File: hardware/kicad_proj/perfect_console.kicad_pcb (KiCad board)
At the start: 2 copper layers, 70 x 95 mm, 71 parts, among them J1 R_Out, J10 PWR_OUT_Pins, J11 GPIO5-7, J12 USB_Out, J13 I2C, J14 ESP_UART, J15 GPIO41, J16 CH_UART, J17 CH_Flash, J18 Micro_SD_Card, J2 Jack_3.5, J3 L_Out, J4 USB, J5 TP4056_WO_Protect, J6 Bat, J7 PWR_Btn, J8 BTN_Pins, J9 PTT_Btn, Q1 NMOS, Q2 NMOS, Q3 NMOS, Q4 NMOS, Q5 NMOS, Q6 NMOS, SW1 Reset, SW2 Boot, U1 ESP32-S3-WROOM1, U2 Display, U3 PCM5102, U4 PAM8403, U5 CH32V006E8R6, U6 LoRa, U7 USBLC6-2SC6, U8 Mic, U9 DC-DC

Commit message: Виправлено імена міток
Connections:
- net DISP_EN renamed DISP_PWR
- net LORA_EN renamed LORA_PWR
- net MIC_EN renamed MIC_PWR
- net POWER_EN renamed BOARD_PWR
- net SPK_EN renamed SPK_PWR
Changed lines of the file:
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@@
 	(net 6 "Net-(Q2-G)")
 	(net 7 "Net-(Q3-G)")
-	(net 8 "DISP_EN")
+	(net 8 "DISP_PWR")
 	(net 9 "VVAL")
 	(net 10 "Net-(J1-Pin_2)")
@@
 	(net 76 "unconnected-(J18-DAT2-Pad1)")
 	(net 77 "unconnected-(J18-DAT1-Pad8)")
-	(net 78 "SPK_EN")
-	(net 79 "LORA_EN")
-	(net 80 "MIC_EN")
-	(net 81 "POWER_EN")
+	(net 78 "SPK_PWR")
+	(net 79 "LORA_PWR")
+	(net 80 "MIC_PWR")
+	(net 81 "BOARD_PWR")
 	(net 82 "Net-(Q1-D)")
 	(net 83 "Net-(Q2-D)")
@@
 			(layers "F.Cu" "F.Paste" "F.Mask")
 			(roundrect_rratio 0.192308)
-			(net 8 "DISP_EN")
+			(net 8 "DISP_PWR")
 			(pintype "passive")
 		)
@@
 			(size 2.3 0.4)
 			(layers "F.Cu" "F.Paste" "F.Mask")
-			(net 80 "MIC_EN")
+			(net 80 "MIC_PWR")
 			(pinfunction "PD7/T2")
 			(pintype "bidirectional")
@@
 			(size 2.3 0.4)
 			(layers "F.Cu" "F.Paste" "F.Mask")
-			(net 8 "DISP_EN")
+			(net 8 "DISP_PWR")
 			(pinfunction "PA4/U2TX")
 			(pintype "bidirectional")
@@
 			(size 2.3 0.4)
 			(layers "F.Cu" "F.Paste" "F.Mask")
-			(net 81 "POWER_EN")
+			(net 81 "BOARD_PWR")
 			(pinfunction "PA5/U2RX_")
 			(pintype "bidirectional")
@@
 			(size 2.3 0.4)
 			(layers "F.Cu" "F.Paste" "F.Mask")
-			(net 79 "LORA_EN")
+			(net 79 "LORA_PWR")
 			(pinfunction "PA0/T1/T2")
 			(pintype "bidirectional")
@@
 			(size 2.3 0.4)
 			(layers "F.Cu" "F.Paste" "F.Mask")
-			(net 78 "SPK_EN")
+			(net 78 "SPK_PWR")
 			(pinfunction "PB3/SWCK")
 			(pintype "bidirectional")
@@
 			(layers "F.Cu" "F.Paste" "F.Mask")
 			(roundrect_rratio 0.05)
-			(net 47 "Net-(J2-L)")
+			(net 46 "Net-(J2-LN)")
 			(pinfunction "LN")
 			(pintype "output")
@@
 			(layers "F.Cu" "F.Paste" "F.Mask")
 			(roundrect_rratio 0.05)
-			(net 46 "Net-(J2-LN)")
+			(net 47 "Net-(J2-L)")
 			(pinfunction "L")
 			(pintype "input")
@@
 			(layers "F.Cu" "F.Paste" "F.Mask")
 			(roundrect_rratio 0.192308)
-			(net 79 "LORA_EN")
+			(net 79 "LORA_PWR")
 			(pintype "passive")
 		)
@@
 			(size 1.6 3)
 			(layers "F.Cu" "F.Paste" "F.Mask")
-			(net 46 "Net-(J2-LN)")
+			(net 47 "Net-(J2-L)")
 			(pinfunction "LEFT")
 			(pintype "output")
@@
 			(layers "F.Cu" "F.Paste" "F.Mask")
 			(roundrect_rratio 0.192308)
-			(net 81 "POWER_EN")
+			(net 81 "BOARD_PWR")
 			(pintype "passive")
 		)
@@
 			(layers "B.Cu" "B.Paste" "B.Mask")
 			(roundrect_rratio 0.192308)
-			(net 78 "SPK_EN")
+			(net 78 "SPK_PWR")
 			(pintype "passive")
 		)
@@
 			(layers "B.Cu" "B.Paste" "B.Mask")
 			(roundrect_rratio 0.192308)
-			(net 80 "MIC_EN")
+			(net 80 "MIC_PWR")
 			(pintype "passive")
 		)
@@
 			(layers "B.Cu" "B.Paste" "B.Mask")
 			(roundrect_rratio 0.192308)
-			(net 81 "POWER_EN")
+			(net 81 "BOARD_PWR")
 			(pintype "passive")
 		)
@@
 			(size 2 4)
 			(layers "B.Cu" "B.Paste" "B.Mask")
-			(net 47 "Net-(J2-L)")
+			(net 46 "Net-(J2-LN)")
 			(pinfunction "L-IN")
 			(pintype "input")
@@
 	)
 	(segment
-		(start 327 166)
-		(end 329 164)
-		(width 0.7)
-		(layer "F.Cu")
-		(net 46)
-	)
-	(segment
-		(start 329 164)
-		(end 329 159.9254)
-		(width 0.7)
-		(layer "F.Cu")
-		(net 46)
-	)
-	(segment
-		(start 329 159.9254)
-		(end 328.293771 159.219171)
-		(width 0.7)
+		(start 332.8 170)
+		(end 318 170)
+		(width 0.9)
 		(layer "F.Cu")
 		(net 46)
 	)
 	(segment
-		(start 314 157.71127)
-		(end 309.63873 153.35)
-		(width 0.7)
+		(start 316 163)
+		(end 317.780829 161.219171)
+		(width 0.9)
 		(layer "F.Cu")
 		(net 46)
 	)
 	(segment
-		(start 307.15 153.35)
-		(end 305.9 154.6)
-		(width 0.7)
+		(start 318 170)
+		(end 316 168)
+		(width 0.9)
 		(layer "F.Cu")
 		(net 46)
 	)
 	(segment
-		(start 309.63873 153.35)
-		(end 307.15 153.35)
-		(width 0.7)
+		(start 317.780829 161.219171)
+		(end 321.093771 161.219171)
+		(width 0.9)
 		(layer "F.Cu")
 		(net 46)
 	)
 	(segment
-		(start 324 166)
-		(end 327 166)
+		(start 321.26 161.21)
+		(end 321.3 161.25)
 		(width 0.7)
 		(layer "F.Cu")
@@
 	)
 	(segment
-		(start 314 160)
-		(end 314 157.71127)
-		(width 0.7)
+		(start 316 168)
+		(end 316 163)
+		(width 0.9)
 		(layer "F.Cu")
 		(net 46)
 	)
 	(via
-		(at 324 166)
+		(at 332.8 170)
 		(size 2)
 		(drill 0.1)
@@
 		(net 46)
 	)
-	(via
-		(at 314 160)
-		(size 2)
-		(drill 0.1)
-		(layers "F.Cu" "B.Cu")
+	(segment
+		(start 332.8 174.575)
+		(end 332.8 170)
+		(width 0.9)
+		(layer "B.Cu")
 		(net 46)
 	)
 	(segment
-		(start 317 166)
-		(end 314 163)
-		(width 0.7)
+		(start 332.75 174.625)
+		(end 332.8 174.575)
+		(width 0.9)
 		(layer "B.Cu")
 		(net 46)
 	)
 	(segment
-		(start 324 166)
-		(end 317 166)
+		(start 327 166)
+		(end 329 164)
 		(width 0.7)
-		(layer "B.Cu")
-		(net 46)
+		(layer "F.Cu")
+		(net 47)
 	)
 	(segment
-		(start 314 163)
-		(end 314 160)
+		(start 329 164)
+		(end 329 159.9254)
 		(width 0.7)
-		(layer "B.Cu")
-		(net 46)
+		(layer "F.Cu")
+		(net 47)
 	)
 	(segment
-		(start 332.8 170)
-		(end 318 170)
-		(width 0.9)
+		(start 329 159.9254)
+		(end 328.293771 159.219171)
+		(width 0.7)
 		(layer "F.Cu")
 		(net 47)
 	)
 	(segment
-		(start 316 163)
-		(end 317.780829 161.219171)
-		(width 0.9)
+		(start 314 157.71127)
+		(end 309.63873 153.35)
+		(width 0.7)
 		(layer "F.Cu")
 		(net 47)
 	)
 	(segment
-		(start 318 170)
-		(end 316 168)
-		(width 0.9)
+		(start 307.15 153.35)
+		(end 305.9 154.6)
+		(width 0.7)
 		(layer "F.Cu")
 		(net 47)
 	)
 	(segment
-		(start 317.780829 161.219171)
-		(end 321.093771 161.219171)
-		(width 0.9)
+		(start 309.63873 153.35)
+		(end 307.15 153.35)
+		(width 0.7)
 		(layer "F.Cu")
 		(net 47)
 	)
 	(segment
-		(start 321.26 161.21)
-		(end 321.3 161.25)
+		(start 324 166)
+		(end 327 166)
 		(width 0.7)
 		(layer "F.Cu")
@@
 	)
 	(segment
-		(start 316 168)
-		(end 316 163)
-		(width 0.9)
+		(start 314 160)
+		(end 314 157.71127)
+		(width 0.7)
 		(layer "F.Cu")
 		(net 47)
 	)
 	(via
-		(at 332.8 170)
+		(at 324 166)
+		(size 2)
+		(drill 0.1)
+		(layers "F.Cu" "B.Cu")
+		(net 47)
+	)
+	(via
+		(at 314 160)
 		(size 2)
 		(drill 0.1)
@@
 	)
 	(segment
-		(start 332.8 174.575)
-		(end 332.8 170)
-		(width 0.9)
+		(start 317 166)
+		(end 314 163)
+		(width 0.7)
 		(layer "B.Cu")
 		(net 47)
 	)
 	(segment
-		(start 332.75 174.625)
-		(end 332.8 174.575)
-		(width 0.9)
+		(start 324 166)
+		(end 317 166)
+		(width 0.7)
+		(layer "B.Cu")
+		(net 47)
+	)
+	(segment
+		(start 314 163)
+		(end 314 160)
+		(width 0.7)
 		(layer "B.Cu")
 		(net 47)

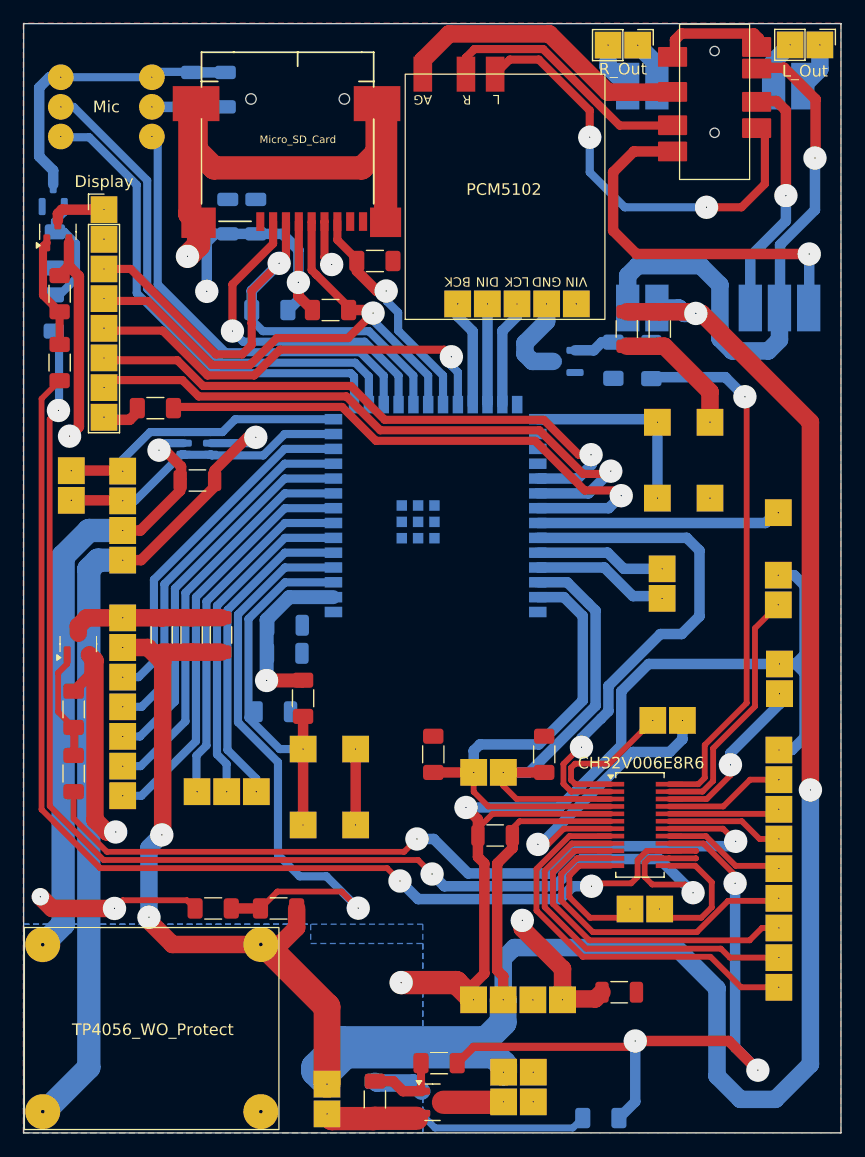
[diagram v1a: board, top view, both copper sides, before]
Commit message: Перепрацьовано схему
Карту пам'яті і дисплей рознесено на окремі шини
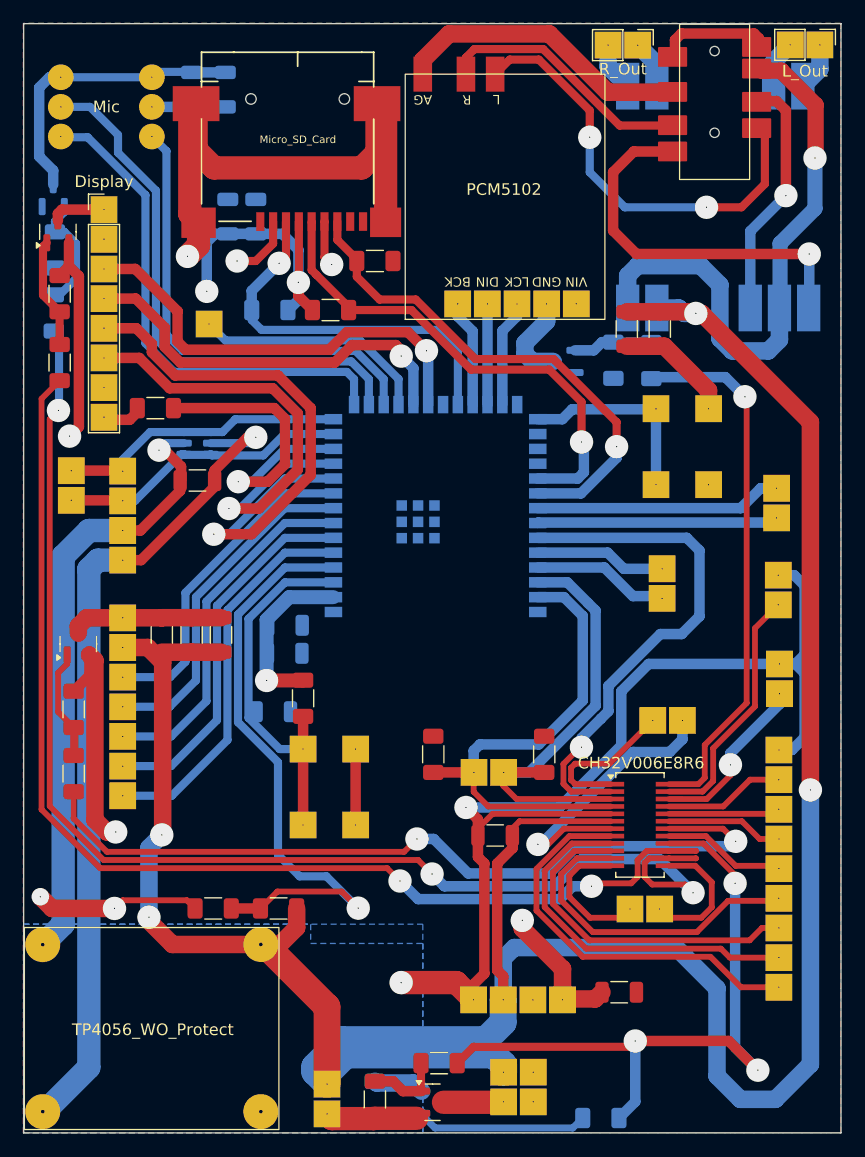
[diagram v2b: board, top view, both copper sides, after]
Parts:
- J11: value GPIO5-7 -> GPIO_40-41; footprint Connector_PinHeader_2.54mm:PinHeader_1x03_P2.54mm_Vertical -> Connector_PinHeader_2.54mm:PinHeader_1x02_P2.54mm_Vertical
- J15: value GPIO41 -> GPIO10
- moved J11 51.6 mm to (330.0, 190.1), turned to 180 degrees
- moved J15 51.4 mm to (281.4, 176.0)
- moved SW2 1.16 mm to (324.2, 189.8)
- renumbered C15 to C14, C16 to C15, U5 to U4, U4 to U5
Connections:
- J11 pad 1: GPIO5 -> GPIO40
- J11 pad 2: GPIO6 -> GPIO41
- J15 pad 1: GPIO41 -> GPIO10
- J18 pad 2: SD_CS -> GND1
- J18 pad 3: HSPI_MOSI -> SD_MOSI
- J18 pad 5: HSPI_SCK -> SD_SCK
- J18 pad 7: HSPI_MISO -> SD_MISO
- R19 pad 2: HSPI_MOSI -> SD_MOSI
- R20 pad 2: HSPI_SCK -> SD_SCK
- R21 pad 2: HSPI_MISO -> SD_MISO
- U1 pad 10: LR_RX -> DISP_RST
- U1 pad 11: LR_TX -> DISP_D/C
- U1 pad 12: LR_AUX -> DISP_BLK
- U1 pad 18: SD_CS -> GPIO10
- U1 pad 19: HSPI_MOSI -> DISP_MOSI
- U1 pad 20: HSPI_SCK -> DISP_SCK
- U1 pad 21: HSPI_MISO -> /DISP_MISO
- U1 pad 22: DISP_CS -> SD_MOSI
- U1 pad 31: DISP_D/C -> SD_SCK
- U1 pad 32: DISP_RST -> SD_MISO
- U1 pad 33: DISP_BLK -> GPIO40
- U1 pad 5: GPIO5 -> LR_M0
- U1 pad 6: GPIO6 -> LR_M1
- U1 pad 7: GPIO7 -> LR_RX
- U1 pad 8: LR_M0 -> LR_TX
- U1 pad 9: LR_M1 -> LR_AUX
- U2 pad 3: HSPI_MOSI -> DISP_SCK
- U2 pad 4: HSPI_SCK -> DISP_MOSI
- U2 pad 5: DISP_CS -> DISP_RST
- U2 pad 7: DISP_RST -> GND1
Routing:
- net HSPI_MOSI: track 51.9 -> 0.00 mm, vias 1 -> 0
- net HSPI_SCK: track 48.1 -> 0.00 mm, vias 1 -> 0
- net SD_MISO: track 0.00 -> 43.9 mm, vias 0 -> 1
- net SD_SCK: track 0.00 -> 42.4 mm, vias 0 -> 1
- net DISP_SCK: track 0.00 -> 38.0 mm, vias 0 -> 1
- net DISP_CS: track 36.9 -> 0.00 mm, vias 1 -> 0
- net DISP_MOSI: track 0.00 -> 35.7 mm, vias 0 -> 1
- net SD_MOSI: track 0.00 -> 33.0 mm, vias 0 -> 1
- net GPIO7: track 30.3 -> 0.00 mm
- net SD_CS: track 29.1 -> 0.00 mm, vias 1 -> 0
- net GPIO6: track 28.7 -> 0.00 mm
- net GPIO5: track 27.7 -> 0.00 mm
- net DISP_BLK: track 49.1 -> 27.9 mm
- net GPIO40: track 0.00 -> 21.2 mm
- net GPIO10: track 0.00 -> 20.4 mm
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
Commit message: Виправлено схему
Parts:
- moved J5 12.6 mm to (265.7, 227.9)
- moved J15 0.10 mm to (281.4, 176.1)
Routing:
- net +3V3: track 47.7 -> 45.9 mm
- net GND1: track 151.9 -> 151.3 mm
- net +4V2: track 244.4 -> 245.0 mm

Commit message: Виправлено печатну плату
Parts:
- moved R4 2.18 mm to (321.2, 178.1), turned to 180 degrees
- moved R5 0.31 mm to (316.1, 179.4)
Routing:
- net SPK_PWR: track 46.2 -> 43.7 mm

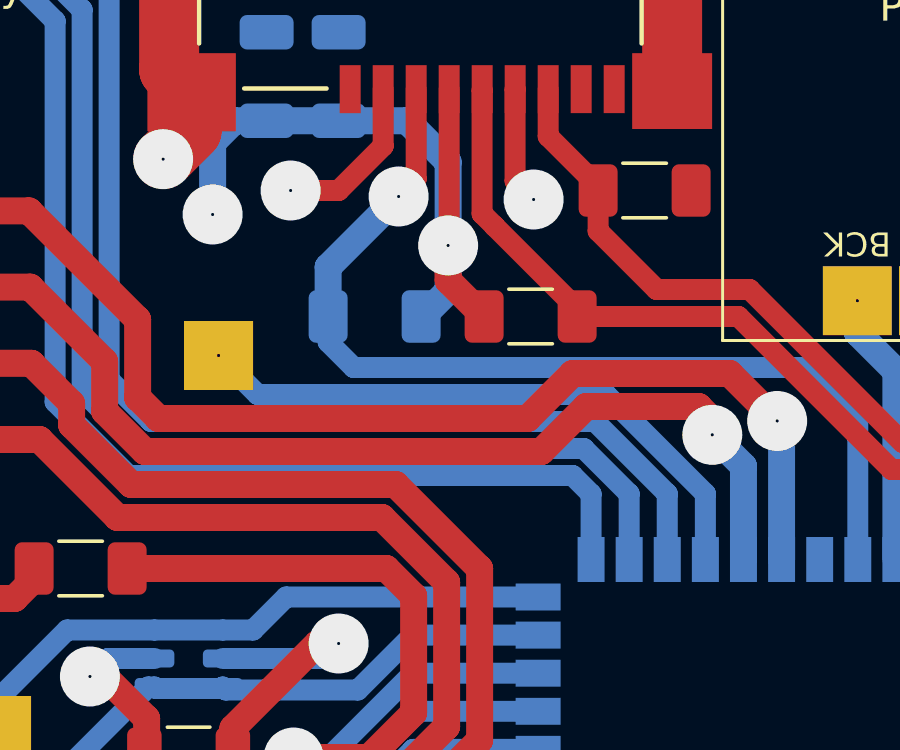
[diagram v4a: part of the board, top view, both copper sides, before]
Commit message: SD_CS пін перенесено на 10 пін ESP32S3
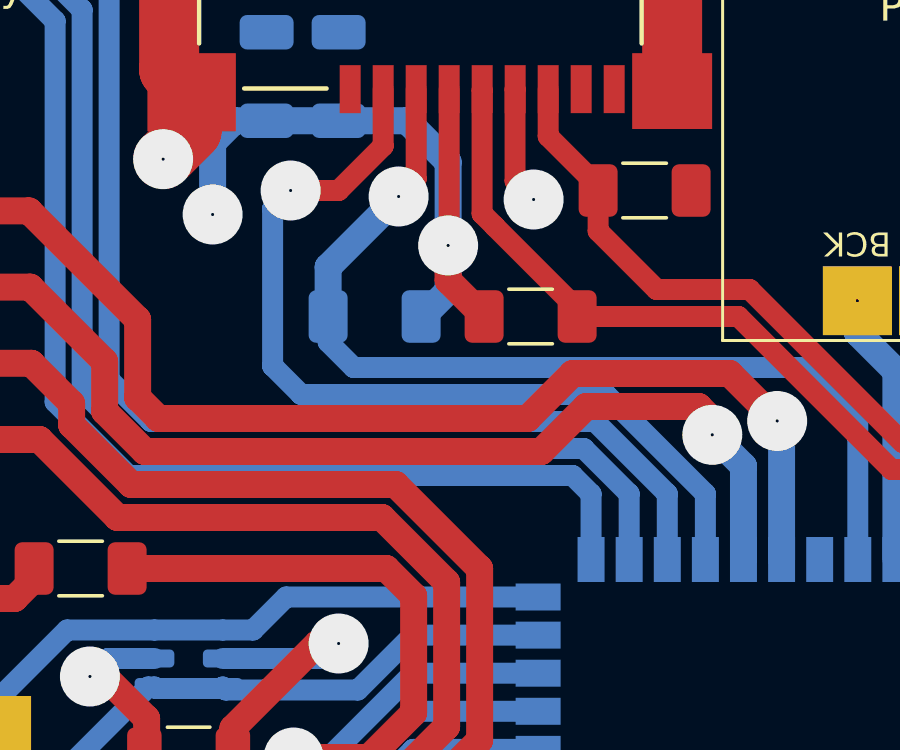
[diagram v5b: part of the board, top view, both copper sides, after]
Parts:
- removed J15: GPIO10, Connector_PinHeader_2.54mm:PinHeader_1x01_P2.54mm_Vertical
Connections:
- J18 pad 2: GND1 -> SD_CS
- U1 pad 18: GPIO10 -> SD_CS
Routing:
- net SD_CS: track 0.00 -> 30.1 mm, vias 0 -> 1
- net GPIO10: track 20.3 -> 0.00 mm
- net GND1: track 151.3 -> 145.7 mm, vias 8 -> 7

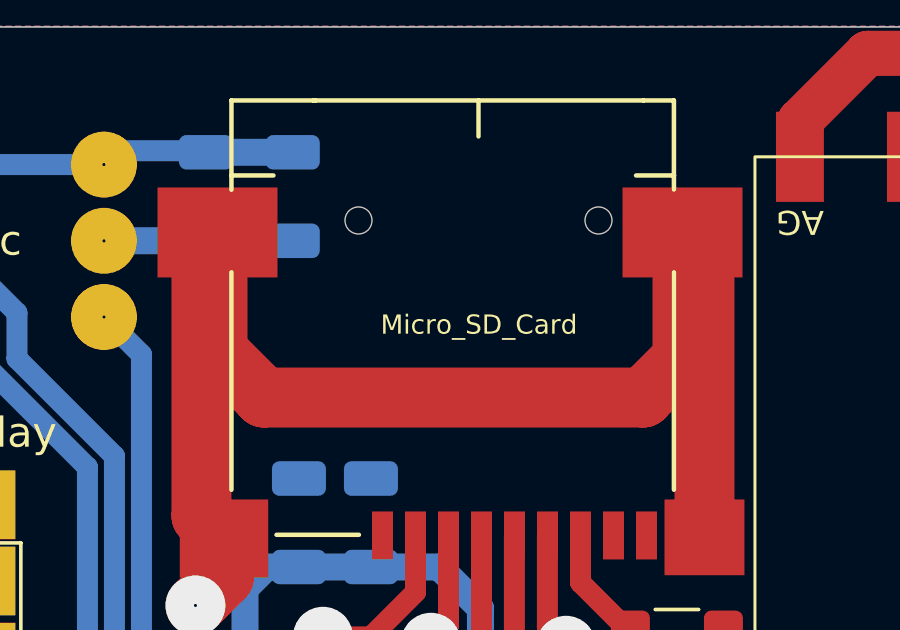
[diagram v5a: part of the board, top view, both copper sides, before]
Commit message: Виправлено зону потенційного КЗ
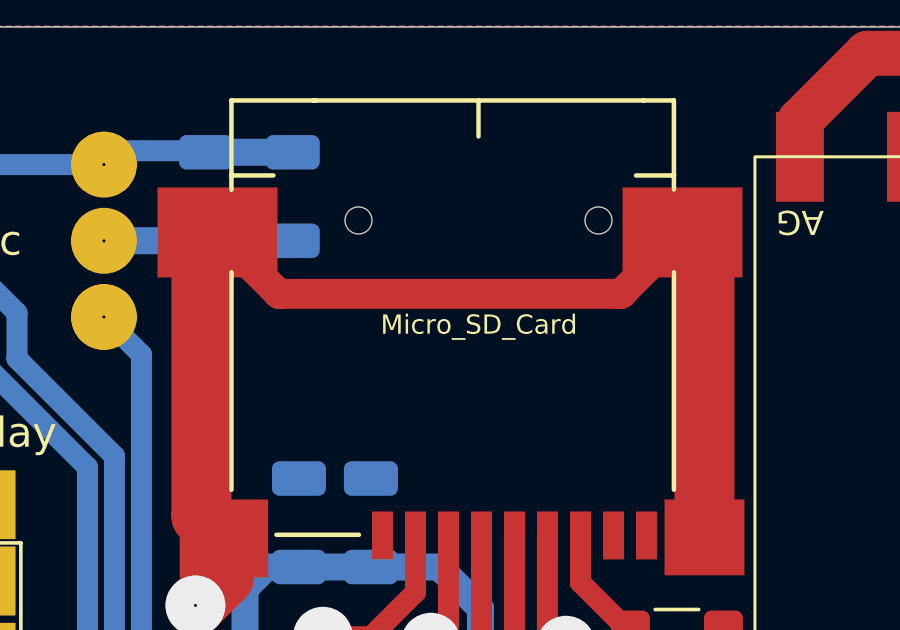
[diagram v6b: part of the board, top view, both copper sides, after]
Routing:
- net GND1: track 145.7 -> 138.0 mm
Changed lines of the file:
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@@
 			(polygon
 				(pts
-					(xy 280.825 163.7) (xy 295.45 163.7) (xy 295.45 165.975) (xy 295.125 165.975) (xy 295.125 166.375)
-					(xy 285.375 166.375) (xy 285.375 167.075) (xy 282.05 167.075) (xy 282.05 165.95) (xy 280.825 165.95)
+					(xy 280.828523 159.668877) (xy 295.453523 159.668877) (xy 295.45 165.975) (xy 295.125 165.975)
+					(xy 295.125 166.375) (xy 285.375 166.375) (xy 285.375 167.075) (xy 282.05 167.075) (xy 282.05 165.95)
+					(xy 280.825 165.95)
 				)
 			)
@@
 	(segment
 		(start 280.284968 157.121855)
-		(end 280.284968 161.084968)
-		(width 2)
-		(layer "F.Cu")
-		(net 67)
-	)
-	(segment
-		(start 280.284968 161.084968)
-		(end 281.825 162.625)
-		(width 2)
+		(end 282.33199 159.168877)
+		(width 1)
 		(layer "F.Cu")
 		(net 67)
@@
 	)
 	(segment
-		(start 294.475 162.625)
-		(end 295.784968 161.315032)
-		(width 2)
+		(start 293.737946 159.168877)
+		(end 295.784968 157.121855)
+		(width 1)
 		(layer "F.Cu")
 		(net 67)
@@
 	)
 	(segment
-		(start 295.784968 161.315032)
-		(end 295.784968 157.121855)
-		(width 2)
+		(start 282.33199 159.168877)
+		(end 293.737946 159.168877)
+		(width 1)
 		(layer "F.Cu")
 		(net 67)
@@
 		(layer "F.Cu")
 		(net 67)
-	)
-	(segment
-		(start 281.825 162.625)
-		(end 294.475 162.625)
-		(width 2)
-		(layer "F.Cu")
-		(net 67)

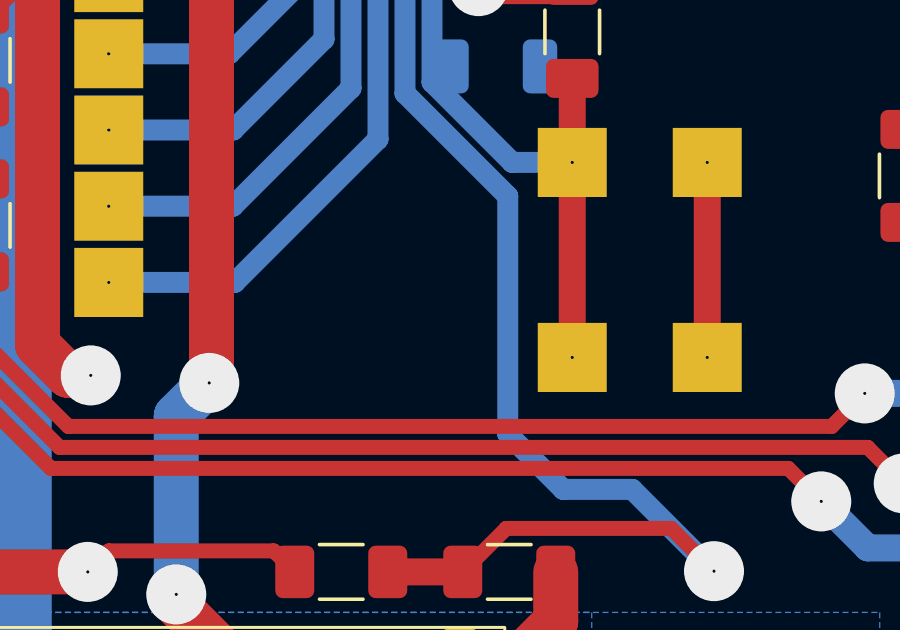
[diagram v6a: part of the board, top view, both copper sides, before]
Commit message: Додано фільтруючий конденсатор на VVAL
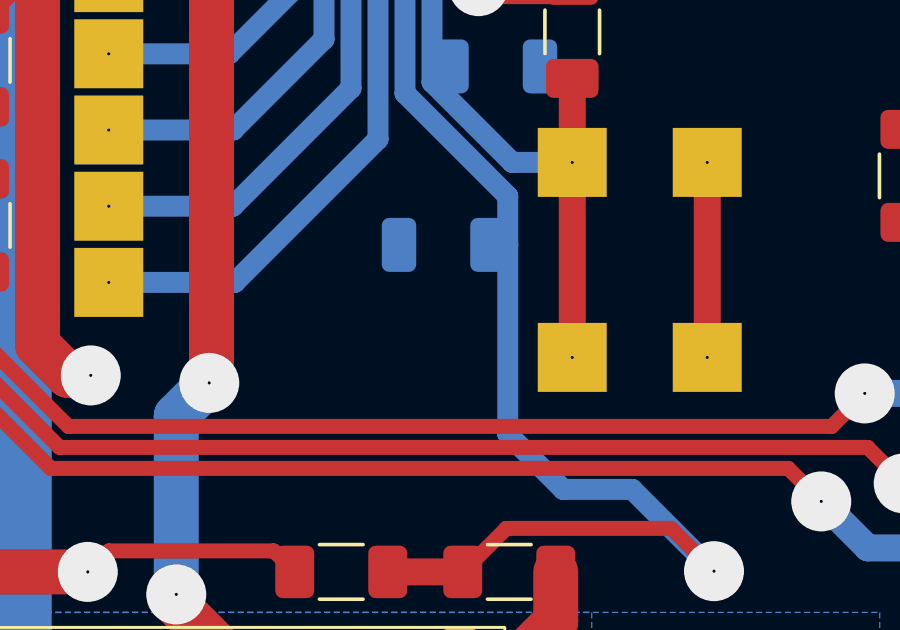
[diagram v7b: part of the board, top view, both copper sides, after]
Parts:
- added C12: 100nF, Capacitor_SMD:C_1206_3216Metric, B.Cu at (285.1, 215.2)
- renumbered C12 to C13, C13 to C14, C14 to C15, C15 to C16, J16 to J15, J17 to J16, J18 to J17
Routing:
- net VVAL: track 52.7 -> 53.3 mm
